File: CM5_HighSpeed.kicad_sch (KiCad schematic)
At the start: 19 parts, among them J10 690-019-298-412, J12 USB3_A, J16 Conn_01x22_Female, J22 690-019-298-412, J5 Conn_01x22_Female, J6 THD-02-R, U12 RT9742SNGV, U6 AP22653W6

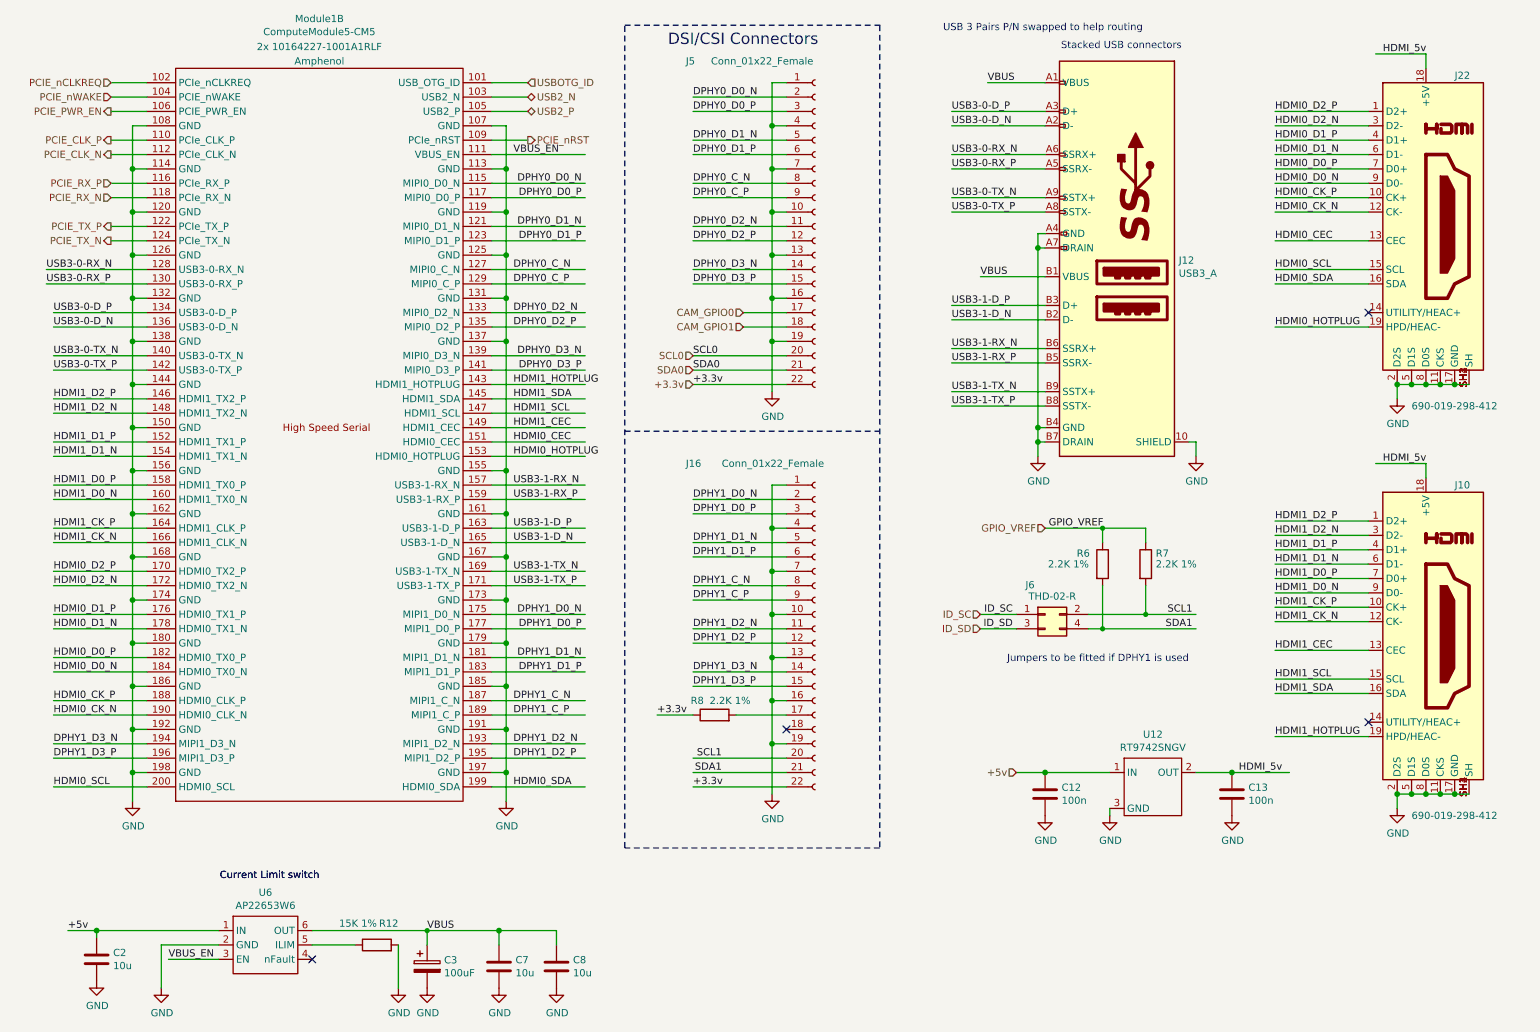
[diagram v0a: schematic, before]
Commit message: remove ethernet, pcie, hdmi
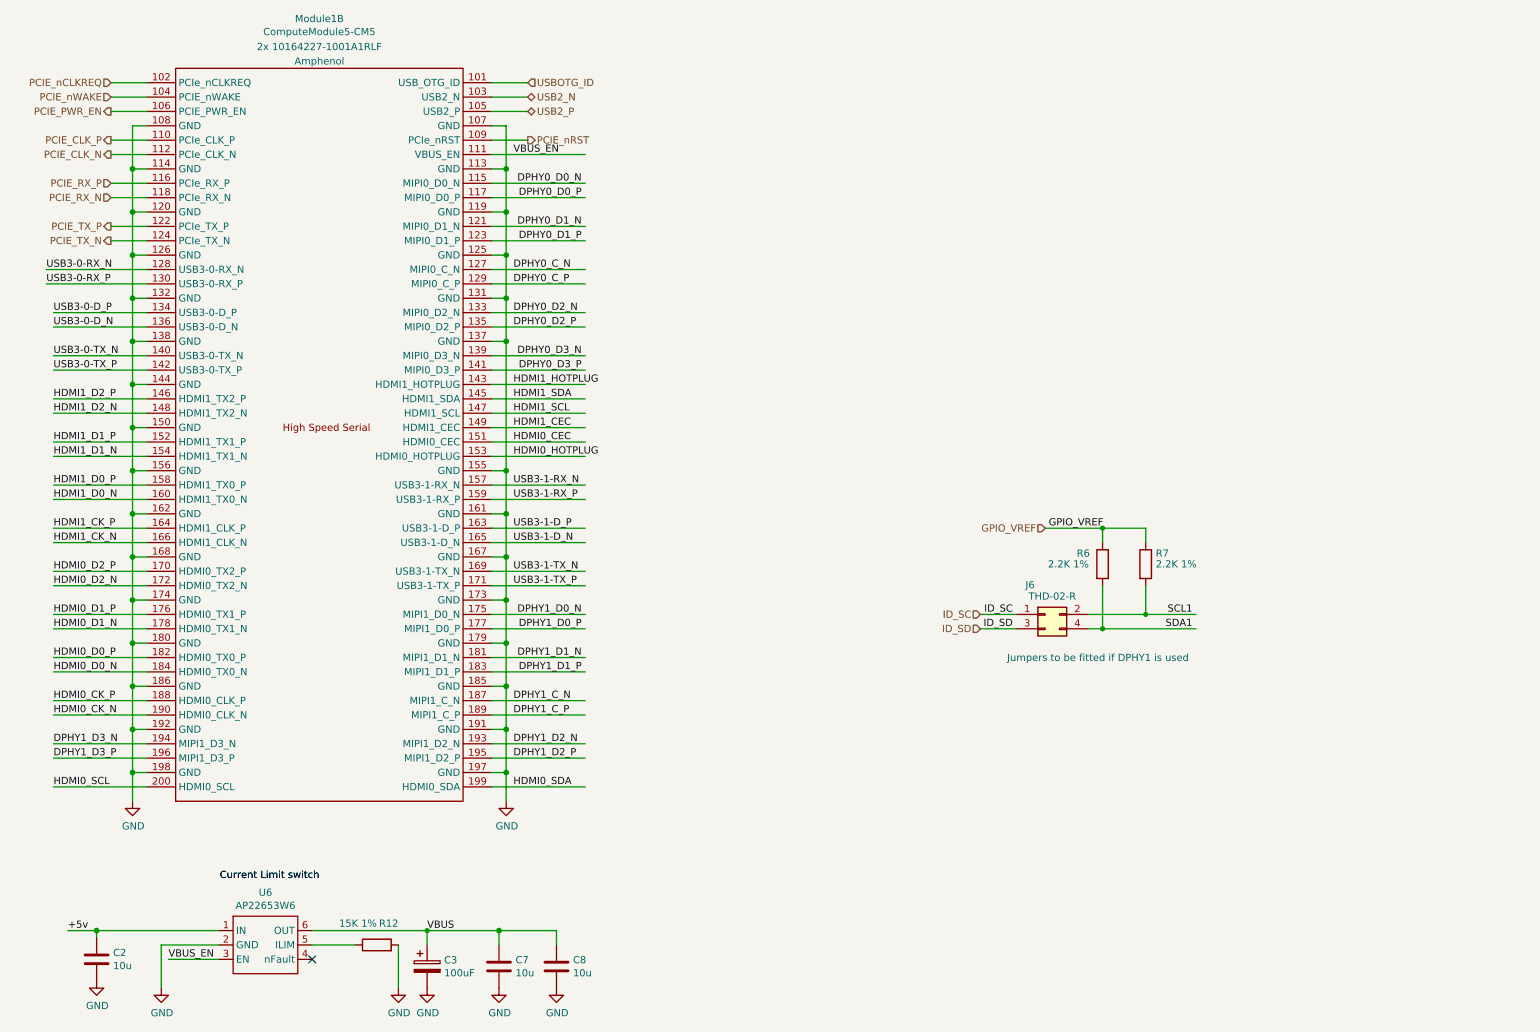
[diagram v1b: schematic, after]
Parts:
- removed C12, C13: 100n, Capacitor_SMD:C_0402_1005Metric, symbol Device:C
- removed J10, J22: 690-019-298-412, CM5IO:EDAC 690-019-298-412, symbol CM5IO:HDMI_A_1.4
- removed J12: USB3_A, CM5IO:MTCONN_UBAF30-D2011, symbol CM5IO:USB3_A
- removed J16, J5: Conn_01x22_Female, CM5IO:Hirose_FH12-22S-0.5SH_1x22-1MP_P0.50mm_Horizontal, symbol Connector:Conn_01x22_Socket
- removed R8: 2.2K 1%, Resistor_SMD:R_0402_1005Metric, symbol Device:R
- removed U12: RT9742SNGV, Package_TO_SOT_SMD:TSOT-23_HandSoldering, symbol CM5IO:RT9742SNGV
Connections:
- no-connect marks 4 -> 1
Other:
- note removed: "DSI/CSI Connectors"
- note removed: "Stacked USB connectors"
- note removed: "USB 3 Pairs P/N swapped to help routing"
